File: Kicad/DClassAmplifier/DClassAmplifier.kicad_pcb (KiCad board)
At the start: 2 copper layers, 135 x 100 mm, 65 parts, among them IC1 DGD05463FN-7, IC2 DGD05463FN-7, J1 Conn_01x02, J2 Conn_01x03, J3 Conn_01x03, J4 Conn_01x02, J5 Conn_01x02, J6 Conn_01x02, Q1 PHP23NQ11T,127, Q2 PHP23NQ11T,127, Q3 PHP23NQ11T,127, Q4 PHP23NQ11T,127, U1 LM319, U2 MAX4016ESA+, U3 AD8567ARUZ

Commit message: Add 10m Resevoir Cap
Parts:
- added C15: 10m, Capacitor_THT:CP_Radial_D18.0mm_P7.50mm, F.Cu at (113.0, 59.7)

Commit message: Combined Board
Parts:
- removed IC1, IC2: DGD05463FN-7, DGD05463:SON50P300X300X80-11N-D
- removed J6: Conn_01x02, TerminalBlock:TerminalBlock_bornier-2_P5.08mm
- added C16: 14u, OutputFilmCapacitor:C4AQLBU5140M18K, F.Cu at (171.2, 107.0)
- added C17: 2.8u, Capacitor_THT:CP_Radial_D8.0mm_P3.50mm, F.Cu at (173.7, 80.0)
- added C18: 2.8u, Capacitor_THT:CP_Radial_D8.0mm_P3.50mm, F.Cu at (173.7, 119.5)
- added JP1: SolderJumper_2_Open, Jumper:SolderJumper-2_P1.3mm_Open_RoundedPad1.0x1.5mm, F.Cu at (115.5, 78.2)
- added JP2: SolderJumper_2_Open, Jumper:SolderJumper-2_P1.3mm_Open_RoundedPad1.0x1.5mm, F.Cu at (104.0, 80.5)
- added JP3: SolderJumper_2_Open, Jumper:SolderJumper-2_P1.3mm_Open_RoundedPad1.0x1.5mm, F.Cu at (103.1, 88.9)
- added JP4: SolderJumper_2_Open, Jumper:SolderJumper-2_P1.3mm_Open_RoundedPad1.0x1.5mm, F.Cu at (112.5, 88.3)
- added R20: 20k, Resistor_SMD:R_0603_1608Metric_Pad0.98x0.95mm_HandSolder, F.Cu at (119.2, 104.2)
- added R21: 10, Resistor_SMD:R_2512_6332Metric_Pad1.40x3.35mm_HandSolder, F.Cu at (126.8, 116.0)
- added R22: 2.2k, Resistor_SMD:R_0603_1608Metric_Pad0.98x0.95mm_HandSolder, F.Cu at (104.0, 95.9)
- added R23: 27k, Resistor_SMD:R_0603_1608Metric_Pad0.98x0.95mm_HandSolder, F.Cu at (101.3, 91.4)
- added R24: 12k, Resistor_SMD:R_0603_1608Metric_Pad0.98x0.95mm_HandSolder, F.Cu at (100.3, 103.5)
- added R25: 12k, Resistor_SMD:R_0603_1608Metric_Pad0.98x0.95mm_HandSolder, F.Cu at (100.3, 102.0)
- added R26: 10k, Resistor_SMD:R_0603_1608Metric_Pad0.98x0.95mm_HandSolder, F.Cu at (108.8, 96.1)
- added R27: 10k, Resistor_SMD:R_0603_1608Metric_Pad0.98x0.95mm_HandSolder, F.Cu at (113.9, 105.1)
- added U4: MAX4016ESA+, MAX4016ESA:MAX4016ESA&plus_, F.Cu at (100.5, 95.9)
- added U5: LM319, Package_SO:SO-14_3.9x8.65mm_P1.27mm, F.Cu at (111.0, 100.6)
- C1: moved to B.Cu
- C10: value 10u -> 10u 50V; footprint Capacitor_SMD:C_0805_2012Metric_Pad1.18x1.45mm_HandSolder -> Capacitor_SMD:C_1206_3216Metric_Pad1.33x1.80mm_HandSolder
- C11: value 56n -> 10u 50V; footprint Capacitor_SMD:C_0603_1608Metric_Pad1.08x0.95mm_HandSolder -> Capacitor_SMD:C_1206_3216Metric_Pad1.33x1.80mm_HandSolder
- C12: value 5.6n -> 10u 50V; footprint Capacitor_SMD:C_0603_1608Metric_Pad1.08x0.95mm_HandSolder -> Capacitor_SMD:C_1206_3216Metric_Pad1.33x1.80mm_HandSolder
- C13: value 47n -> 100n
- C14: value 4.7n -> 10n
- C15: value 10m -> 100n; footprint Capacitor_THT:CP_Radial_D18.0mm_P7.50mm -> Capacitor_SMD:C_0603_1608Metric_Pad1.08x0.95mm_HandSolder
- C2: value 2.8u -> 10m; footprint Capacitor_THT:CP_Radial_D8.0mm_P3.50mm -> Capacitor_THT:CP_Radial_D18.0mm_P7.50mm
- C3: value 14u -> 100n; footprint OutputFilmCapacitor:C4AQQBW5140A3JJ -> Capacitor_SMD:C_0603_1608Metric_Pad1.08x0.95mm_HandSolder
- C4: value 2.8u -> 47n; footprint Capacitor_THT:CP_Radial_D8.0mm_P3.50mm -> Capacitor_SMD:C_0603_1608Metric_Pad1.08x0.95mm_HandSolder
- C5: value 10n -> 10u; footprint Capacitor_SMD:C_0201_0603Metric_Pad0.64x0.40mm_HandSolder -> Capacitor_SMD:C_0603_1608Metric_Pad1.08x0.95mm_HandSolder
- C6: value 10u 50V -> 4.7n; footprint Capacitor_SMD:C_1206_3216Metric_Pad1.33x1.80mm_HandSolder -> Capacitor_SMD:C_0603_1608Metric_Pad1.08x0.95mm_HandSolder
- C7: value 10u 50V -> 56n; footprint Capacitor_SMD:C_1206_3216Metric_Pad1.33x1.80mm_HandSolder -> Capacitor_SMD:C_0603_1608Metric_Pad1.08x0.95mm_HandSolder
- C8: value 10u 50V -> 5.6n; footprint Capacitor_SMD:C_1206_3216Metric_Pad1.33x1.80mm_HandSolder -> Capacitor_SMD:C_0603_1608Metric_Pad1.08x0.95mm_HandSolder
- J3: value Conn_01x03 -> Conn_01x02; footprint TerminalBlock:TerminalBlock_bornier-3_P5.08mm -> TerminalBlock:TerminalBlock_bornier-2_P5.08mm
- L1, L2: footprint 1422455C:1422455C -> HCTI-220-5.8:IND_HCTI-220-5.8
- Q1, Q2, Q3, Q4: footprint Package_TO_SOT_THT:TO-220-3_Vertical -> Package_TO_SOT_THT:TO-220-3_Horizontal_TabDown
- R1, R14: value 10k -> 1Meg
- R10: value 10 -> 750; footprint Resistor_SMD:R_2512_6332Metric_Pad1.40x3.35mm_HandSolder -> Resistor_SMD:R_0603_1608Metric_Pad0.98x0.95mm_HandSolder
- R11, R9: value 10 -> 10k; footprint Resistor_SMD:R_2512_6332Metric_Pad1.40x3.35mm_HandSolder -> Resistor_SMD:R_0603_1608Metric_Pad0.98x0.95mm_HandSolder
- R12: value 10 -> 1k; footprint Resistor_SMD:R_2512_6332Metric_Pad1.40x3.35mm_HandSolder -> Resistor_SMD:R_0603_1608Metric_Pad0.98x0.95mm_HandSolder
- R13, R2: value 10k -> 1k
- R15: value 16k -> 1Meg
- R16: value 10k -> 10; footprint Resistor_SMD:R_0603_1608Metric_Pad0.98x0.95mm_HandSolder -> Resistor_SMD:R_2512_6332Metric_Pad1.40x3.35mm_HandSolder
- R17: value 750 -> 20k
- R18: value 22k -> 10; footprint Resistor_SMD:R_0603_1608Metric_Pad0.98x0.95mm_HandSolder -> Resistor_SMD:R_2512_6332Metric_Pad1.40x3.35mm_HandSolder
- R19: value 620 -> 10; footprint Resistor_SMD:R_0603_1608Metric_Pad0.98x0.95mm_HandSolder -> Resistor_SMD:R_2512_6332Metric_Pad1.40x3.35mm_HandSolder
- R3: value 27k -> 1k
- R4: value 2.2k -> 1Meg
- R5: value 12k -> 16k
- R6: value 12k -> 10k
- R7: value 20k -> 22k
- R8: value 20k -> 620
- TP1, TP10, TP2, TP3, TP4, TP5, TP6, TP7, TP8, TP9: footprint TestPoint:TestPoint_Pad_D2.0mm -> TestPoint:TestPoint_THTPad_D1.5mm_Drill0.7mm
- U1: value LM319 -> AD8567ARUZ; footprint Package_SO:SO-14_3.9x8.65mm_P1.27mm -> AD8567ARUZ:AD8567ARUZ
- U2: value MAX4016ESA+ -> DGD05463FN-7; footprint MAX4016ESA:MAX4016ESA&plus_ -> DGD05463:SON50P300X300X80-11N-D
- U3: value AD8567ARUZ -> DGD05463FN-7; footprint AD8567ARUZ:AD8567ARUZ -> DGD05463:SON50P300X300X80-11N-D
- moved C14 332.6 mm to (100.3, 100.4), turned to 180 degrees
- moved R13 324.2 mm to (112.5, 90.3), turned to 180 degrees
- moved R14 323.3 mm to (99.6, 88.9), turned to 90 degrees
- moved R15 322.3 mm to (110.0, 89.4), turned to 90 degrees
- moved U1 321.0 mm to (109.1, 84.1)
- moved C13 320.9 mm to (102.8, 101.3), turned to 270 degrees
- moved TP10 316.8 mm to (110.2, 78.4)
- moved C11 314.0 mm to (120.7, 111.2), turned to 90 degrees
- moved J2 313.8 mm to (99.0, 109.9), turned to 270 degrees
- moved J5 313.4 mm to (99.0, 69.0), turned to 270 degrees
- moved R19 311.6 mm to (126.8, 105.8), turned to 270 degrees
- moved R1 309.9 mm to (106.4, 79.3), turned to 270 degrees
- moved R17 308.3 mm to (119.2, 92.4)
- moved R2 308.0 mm to (104.0, 78.4)
- moved U3 307.5 mm to (119.7, 106.8), turned to 180 degrees
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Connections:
- C10 pad 1: Net-(C10-Pad1) -> /OutputFilter/SIG+
- C10 pad 2: /LPF/SIG_IN -> Net-(C10-Pad2)
- C11 pad 1: Net-(C11-Pad1) -> GND
- C11 pad 2: /Comparator/SIG_IN -> VCC
- C12 pad 1: Net-(C12-Pad1) -> /OutputFilter/SIG-
- C12 pad 2: GND -> Net-(C12-Pad2)
- C13 pad 1: /LPF/Filter_FirstStage -> VCC
- C13 pad 2: Net-(C13-Pad2) -> GND
- C14 pad 1: Net-(C14-Pad1) -> /Comparator/TRIANGLE_IN
- C14 pad 2: GND -> Net-(C14-Pad2)
- C15 pad 1: VDD -> VCC
- C15 pad 2: GNDPWR -> GND
- C2 pad 1: /OutputFilter/SPEAKER+ -> VDD
- C3 pad 1: /OutputFilter/SPEAKER- -> VCC
- C3 pad 2: /OutputFilter/SPEAKER+ -> GND
- C4 pad 1: /OutputFilter/SPEAKER- -> Net-(C4-Pad1)
- C4 pad 2: GNDPWR -> Net-(C4-Pad2)
- C5 pad 1: /Comparator/TRIANGLE_IN -> Net-(C5-Pad1)
- C5 pad 2: Net-(C5-Pad2) -> /SIG_IN
- C6 pad 1: GND -> Net-(C6-Pad1)
- C6 pad 2: VCC -> GND
- C7 pad 1: GND -> Net-(C7-Pad1)
- C7 pad 2: VCC -> Net-(C7-Pad2)
- C8 pad 1: /OutputFilter/SIG+ -> Net-(C8-Pad1)
- C8 pad 2: Net-(C8-Pad2) -> GND
- C9 pad 1: /OutputFilter/SIG- -> GND
- C9 pad 2: Net-(C9-Pad2) -> VCC
- J1 pad 1: /OutputFilter/SPEAKER+ -> VDD
- J1 pad 2: /OutputFilter/SPEAKER- -> GNDPWR
- J3 pad 1: /H-Bridge/PWM -> VCC
- J3 pad 2: /H-Bridge/INV_PWM -> GND
- J4 pad 1: VDD -> /OutputFilter/SPEAKER-
- J4 pad 2: GND -> /OutputFilter/SPEAKER+
- J5 pad 1: /LPF/SIG_IN -> /SIG_IN
- R1 pad 1: VCC -> /LPF/BIASED_SIG
- R1 pad 2: /H-Bridge/PWM -> GND
- R10 pad 1: Net-(Q4-Pad1) -> /LPF/Filter_FirstStage
- R10 pad 2: Net-(IC2-Pad10) -> Net-(C7-Pad1)
- R11 pad 1: Net-(Q1-Pad1) -> Net-(R11-Pad1)
- R11 pad 2: Net-(IC1-Pad3) -> GND
- R12 pad 1: Net-(Q3-Pad1) -> Net-(JP3-Pad2)
- R12 pad 2: Net-(IC2-Pad3) -> /LPF/VREF
- R13 pad 1: VCC -> Net-(C7-Pad2)
- R13 pad 2: Net-(R13-Pad2) -> /Comparator/SIG_IN
- R14 pad 1: Net-(R13-Pad2) -> /LPF/VREF
- R15 pad 1: /LPF/VREF -> /Comparator/SIG_IN
- R15 pad 2: Net-(C10-Pad1) -> GND
- R16 pad 1: Net-(C11-Pad1) -> Net-(Q1-Pad1)
- R16 pad 2: Net-(C12-Pad1) -> Net-(R16-Pad2)
- R17 pad 1: /LPF/Filter_FirstStage -> /H-Bridge/V_DT1
- R17 pad 2: Net-(C11-Pad1) -> GND
- R18 pad 1: Net-(C13-Pad2) -> Net-(Q2-Pad1)
- R18 pad 2: Net-(C14-Pad1) -> Net-(R18-Pad2)
- R19 pad 1: /LPF/BIASED_SIG -> Net-(Q3-Pad1)
- R19 pad 2: Net-(C13-Pad2) -> Net-(R19-Pad2)
- R2 pad 1: VCC -> Net-(JP2-Pad2)
- R2 pad 2: /H-Bridge/INV_PWM -> /LPF/BIASED_SIG
- R3 pad 1: Net-(R3-Pad1) -> Net-(C4-Pad1)
- R3 pad 2: Net-(R3-Pad2) -> /LPF/Filter_FirstStage
- R4 pad 1: Net-(C5-Pad2) -> GND
- R4 pad 2: Net-(R3-Pad1) -> Net-(C4-Pad1)
- R5 pad 1: Net-(R3-Pad2) -> /LPF/VREF
- R5 pad 2: /Comparator/TRIANGLE_IN -> Net-(C5-Pad1)
- R6 pad 1: Net-(R3-Pad2) -> VCC
- R6 pad 2: /Comparator/TRIANGLE_IN -> Net-(R11-Pad1)
- R7 pad 1: /H-Bridge/V_DT1 -> Net-(C4-Pad2)
- R7 pad 2: GND -> Net-(C6-Pad1)
- R8 pad 1: /H-Bridge/V_DT2 -> /LPF/BIASED_SIG
- R8 pad 2: GND -> Net-(C4-Pad2)
- R9 pad 1: Net-(Q2-Pad1) -> Net-(C7-Pad1)
- R9 pad 2: Net-(IC1-Pad10) -> Net-(C8-Pad1)
- TP2 pad 1: /Comparator/SIG_IN -> /H-Bridge/INV_PWM
- TP3 pad 1: /Comparator/TRIANGLE_IN -> /H-Bridge/PWM
- TP4 pad 1: /H-Bridge/PWM -> /Comparator/TRIANGLE_IN
- TP5 pad 1: /H-Bridge/INV_PWM -> /OutputFilter/SIG+
- TP6 pad 1: /OutputFilter/SIG+ -> /OutputFilter/SPEAKER+
- TP7 pad 1: /OutputFilter/SIG- -> /OutputFilter/SPEAKER-
- TP8 pad 1: /OutputFilter/SPEAKER+ -> /OutputFilter/SIG-
- TP9 pad 1: /OutputFilter/SPEAKER- -> /Comparator/SIG_IN
- U1 pad 1: Net-(U1-Pad1) -> /LPF/BIASED_SIG
- U1 pad 10: /Comparator/SIG_IN -> Net-(C8-Pad1)
- U1 pad 11: VCC -> GND
- U1 pad 12: /H-Bridge/PWM -> Net-(C6-Pad1)
- U1 pad 13: Net-(U1-Pad13) -> Net-(C4-Pad1)
- U1 pad 14: Net-(U1-Pad14) -> /LPF/Filter_FirstStage
- U1 pad 2: Net-(U1-Pad2) -> Net-(JP2-Pad2)
- U1 pad 3: GND -> Net-(C5-Pad1)
- U1 pad 4: /Comparator/SIG_IN -> VCC
- U1 pad 5: /Comparator/TRIANGLE_IN -> Net-(R11-Pad1)
- U1 pad 6: GND -> Net-(JP3-Pad2)
- U1 pad 7: /H-Bridge/INV_PWM -> /LPF/VREF
- U1 pad 8: GND -> /Comparator/SIG_IN
- U1 pad 9: /Comparator/TRIANGLE_IN -> Net-(C7-Pad2)
- U2 pad 1: Net-(R3-Pad1) -> VCC
- U2 pad 2: /LPF/VREF -> Net-(C10-Pad2)
- U2 pad 3: Net-(R3-Pad2) -> Net-(R16-Pad2)
- U2 pad 4: GND -> /OutputFilter/SIG+
- U2 pad 5: /LPF/VREF -> Net-(U2-Pad5)
- U2 pad 6: Net-(C5-Pad2) -> /H-Bridge/V_DT1
- U2 pad 7: /Comparator/TRIANGLE_IN -> VCC
- U2 pad 8: VCC -> /H-Bridge/PWM
- U3 pad 1: /LPF/VREF -> VCC
- U3 pad 10: Net-(C12-Pad1) -> Net-(R21-Pad2)
- U3 pad 11: GND -> Net-(U3-Pad11)
- U3 pad 2: /LPF/VREF -> Net-(C12-Pad2)
- U3 pad 3: Net-(R13-Pad2) -> Net-(R19-Pad2)
- U3 pad 4: VCC -> /OutputFilter/SIG-
- U3 pad 5: Net-(C10-Pad1) -> Net-(U3-Pad5)
- U3 pad 6: /LPF/BIASED_SIG -> /H-Bridge/V_DT2
- U3 pad 7: /LPF/BIASED_SIG -> VCC
- U3 pad 8: /Comparator/SIG_IN -> /H-Bridge/INV_PWM
- U3 pad 9: /Comparator/SIG_IN -> GND
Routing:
- net VCC: track 0.00 -> 143.7 mm, vias 0 -> 9
- net /H-Bridge/PWM: track 0.00 -> 32.5 mm, vias 0 -> 2
- net /LPF/VREF: track 0.00 -> 28.9 mm, vias 0 -> 2
- net /H-Bridge/INV_PWM: track 0.00 -> 28.3 mm
- net /LPF/BIASED_SIG: track 0.00 -> 23.8 mm, vias 0 -> 2
- net /Comparator/TRIANGLE_IN: track 0.00 -> 22.7 mm
- net /LPF/Filter_FirstStage: track 0.00 -> 20.2 mm, vias 0 -> 2
- net /Comparator/SIG_IN: track 0.00 -> 19.4 mm, vias 0 -> 2
- net /SIG_IN: track 0.00 -> 17.2 mm
- net GNDPWR: track 0.00 -> 16.2 mm
- net Net-(R21-Pad2): track 0.00 -> 16.2 mm
- net GND: track 0.00 -> 15.2 mm, vias 0 -> 10
- net Net-(R18-Pad2): track 0.00 -> 14.9 mm
- net Net-(R16-Pad2): track 0.00 -> 14.1 mm, vias 0 -> 2
- net Net-(R23-Pad2): track 0.00 -> 13.8 mm
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- added copper zone on F.Cu, net /OutputFilter/SIG+
- added copper zone on F.Cu, net /OutputFilter/SIG-
- added copper zone on F.Cu, net /OutputFilter/SPEAKER+
- added copper zone on F.Cu, net /OutputFilter/SPEAKER-
- added copper zone on B.Cu, net GND
- added copper zone on F.Cu, net GND
- added copper zone on B.Cu, net GNDPWR
- added copper zone on F.Cu, net GNDPWR
- added copper zone on B.Cu, net VDD
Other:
- board size 135 x 100 mm -> 100 x 75 mm
- board text added: "ECEN405 80W D Class Amplifier REV 1.0 13/08/21 Sharon McTaggart Josh Benfell Saul Ramsay"

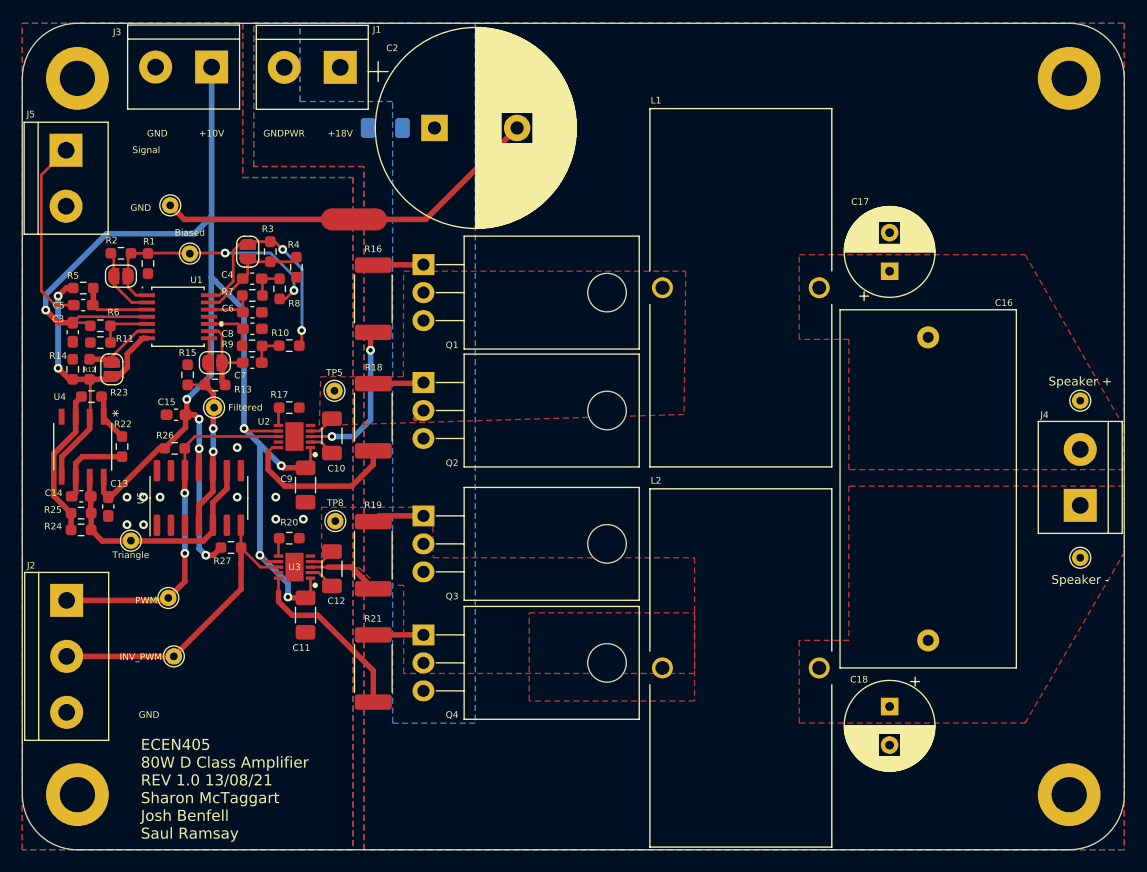
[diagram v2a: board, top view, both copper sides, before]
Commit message: Add 10V Reg and Reroute
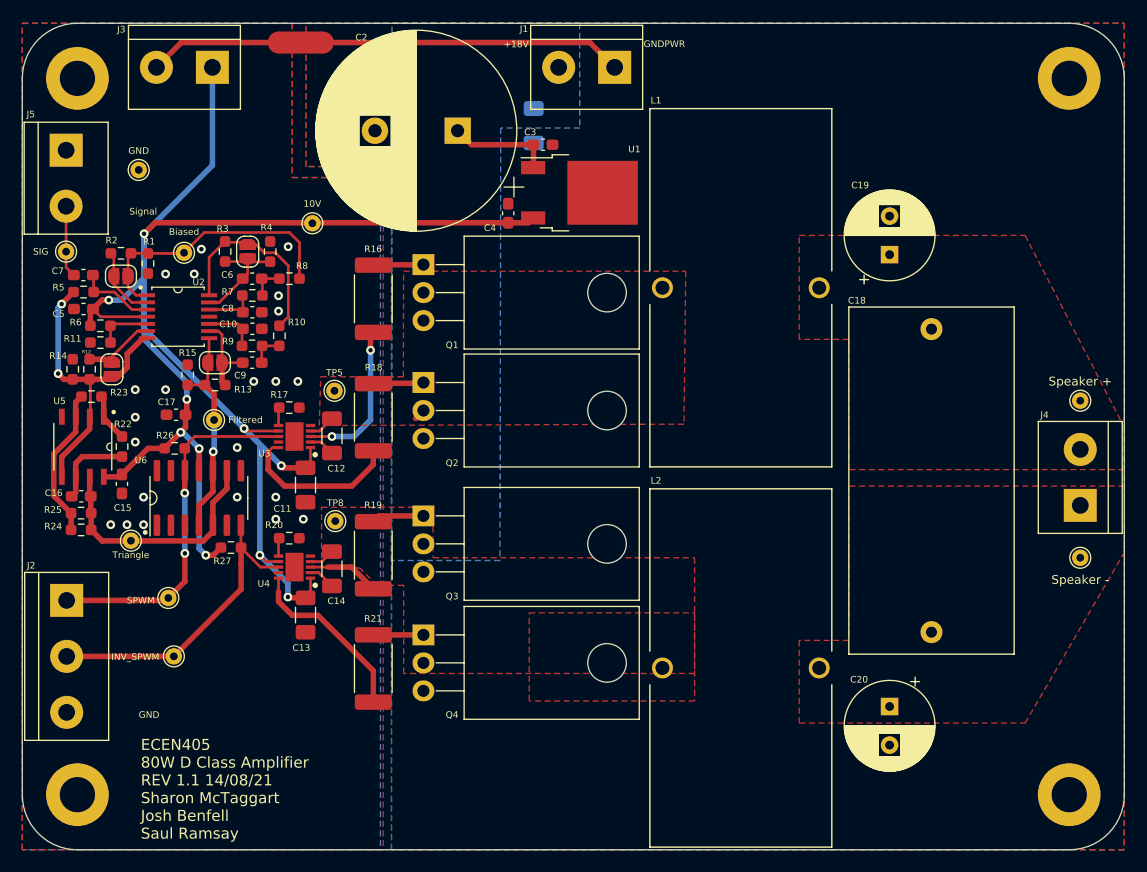
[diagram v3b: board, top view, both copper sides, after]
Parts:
- removed the C16 at (171.2, 107.0)
- removed the U4 at (100.5, 95.9)
- added C18: 14u, OutputFilmCapacitor:C4AQLBU5140M18K, F.Cu at (171.5, 106.2)
- added C3: 330n, Capacitor_SMD:C_0603_1608Metric_Pad1.08x0.95mm_HandSolder, F.Cu at (142.2, 68.5)
- added C4: 100n, Capacitor_SMD:C_0603_1608Metric_Pad1.08x0.95mm_HandSolder, F.Cu at (139.1, 74.7)
- added G***: LOGO, Fry:Fry, B.Cu at (162.2, 97.1)
- added TP11: TestPoint, TestPoint:TestPoint_THTPad_D1.5mm_Drill0.7mm, F.Cu at (121.3, 75.7)
- added TP12: TestPoint, TestPoint:TestPoint_THTPad_D1.5mm_Drill0.7mm, F.Cu at (99.0, 78.2)
- added U2: AD8567ARUZ, AD8567ARUZ:AD8567ARUZ, F.Cu at (109.1, 84.1)
- added U5: MAX4016ESA+, MAX4016ESA:MAX4016ESA&plus_, F.Cu at (100.5, 95.9)
- U1: value AD8567ARUZ -> L78M10ABDT; footprint AD8567ARUZ:AD8567ARUZ -> Package_TO_SOT_SMD:TO-252-2
- moved U1 38.1 mm to (145.6, 72.9)
- moved J1 24.9 mm to (148.8, 61.5)
- moved NT1 16.8 mm to (120.3, 59.2)
- moved C1 13.5 mm to (141.4, 66.8), turned to 90 degrees
- moved TP1 4.31 mm to (105.6, 70.8)
- moved R3 4.10 mm to (113.4, 78.2)
- moved R4 2.77 mm to (117.5, 78.2), turned to 270 degrees
- moved C7 2.73 mm to (100.5, 80.3)
- moved C15 2.40 mm to (104.0, 99.3)
- moved C5 2.32 mm to (100.5, 83.4), turned to 180 degrees
- moved C2 2.11 mm to (134.5, 67.2), turned to 180 degrees
- moved C19 1.50 mm to (173.7, 78.5)
- moved R8 1.28 mm to (119.2, 80.7), turned to 180 degrees
- moved R10 1.26 mm to (118.3, 85.9), turned to 270 degrees
- moved TP9 1.12 mm to (112.4, 93.5)
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- renumbered C8 to C10, C9 to C11, C10 to C12, C11 to C13, C12 to C14, C13 to C15, C14 to C16, C15 to C17, C17 to C19, C18 to C20, C3 to C5, C4 to C6, C5 to C7, C6 to C8, C7 to C9, U2 to U3, U3 to U4, U5 to U6
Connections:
- C10 pad 1: Net-(C8-Pad1) -> Net-(C10-Pad1)
- C6 pad 1: Net-(C4-Pad1) -> Net-(C6-Pad1)
- C7 pad 1: Net-(C5-Pad1) -> Net-(C7-Pad1)
- C8 pad 1: Net-(C6-Pad1) -> Net-(C8-Pad1)
- C9 pad 2: Net-(C7-Pad2) -> Net-(C9-Pad2)
- J1 pad 1: VDD -> GNDPWR
- J1 pad 2: GNDPWR -> VDD
- J5 pad 1: /SIG_IN -> GND
- J5 pad 2: GND -> /SIG_IN
- JP1 pad 2: Net-(C4-Pad1) -> Net-(C6-Pad1)
- JP4 pad 2: Net-(C7-Pad2) -> Net-(C9-Pad2)
- R13 pad 1: Net-(C7-Pad2) -> Net-(C9-Pad2)
- R3 pad 1: Net-(C4-Pad1) -> Net-(C6-Pad1)
- R4 pad 2: Net-(C4-Pad1) -> Net-(C6-Pad1)
- R5 pad 2: Net-(C5-Pad1) -> Net-(C7-Pad1)
- R7 pad 2: Net-(C6-Pad1) -> Net-(C8-Pad1)
- R9 pad 2: Net-(C8-Pad1) -> Net-(C10-Pad1)
- U1 pad 1: /LPF/BIASED_SIG -> VDD
- U1 pad 2: Net-(JP2-Pad2) -> GNDPWR
- U1 pad 3: Net-(C5-Pad1) -> VCC
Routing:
- net VCC: track 143.7 -> 166.8 mm, vias 9 -> 10
- net GNDPWR: track 16.2 -> 27.4 mm
- net Net-(C4-Pad1): track 10.7 -> 0.00 mm
- net /SIG_IN: track 17.2 -> 6.54 mm
- net VDD: track 0.00 -> 9.51 mm
- net Net-(C9-Pad2): track 0.00 -> 7.87 mm
- net Net-(C7-Pad2): track 7.87 -> 0.00 mm
- net Net-(C7-Pad1): track 0.00 -> 7.07 mm
- net Net-(C5-Pad1): track 6.66 -> 0.00 mm
- net Net-(C6-Pad1): track 4.71 -> 10.3 mm
- net Net-(C10-Pad1): track 0.00 -> 4.83 mm
- net GND: track 15.2 -> 12.0 mm, vias 10 -> 22
- net /LPF/Filter_FirstStage: track 20.2 -> 17.9 mm, vias 2 -> 0
- net /LPF/BIASED_SIG: track 23.8 -> 24.9 mm, vias 2 -> 0
- net /Comparator/SIG_IN: track 19.4 -> 19.6 mm, vias 2 -> 1
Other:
- board text added: "ECEN405 80W D Class Amplifier REV 1.1 14/08/21 Sharon McTaggart Josh Benfell Saul Ramsay"
- board text added: "The D Class Amplifier at home"
- board text removed: "ECEN405 80W D Class Amplifier REV 1.0 13/08/21 Sharon McTaggart Josh Benfell Saul Ramsay"

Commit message: Graphics and SilkScreen Improvement
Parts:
- added REF**: Sinusoid, Graphics:Sinusoid, F.Cu at (96.8, 76.2)
- added REF**: GND, Graphics:GND, F.Cu at (104.0, 68.4)
- added REF**: SPWM, Graphics:SPWM, F.Cu at (106.5, 116.7)
- added REF**: Triangle, Graphics:Triangle, F.Cu at (104.5, 103.2)
- added REF**: GND, Graphics:GND, F.Cu at (112.0, 68.5)
- added REF**: SPWM, Graphics:SPWM, F.Cu at (105.7, 108.0)
- moved TP1 7.47 mm to (112.2, 67.4)
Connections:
- J3 pad 1: VCC -> GND
- J3 pad 2: GND -> VCC
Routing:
- net VCC: track 166.8 -> 149.2 mm
- net GND: track 12.0 -> 6.95 mm
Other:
- board text added: "+10V"
